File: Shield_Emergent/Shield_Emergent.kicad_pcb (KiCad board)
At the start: 2 copper layers, 33.4 x 63.5 mm, 23 parts, among them J1 Conn_01x02_Female, J2 Conn_01x04_Male, J3 Conn_01x02_Female, J4 Conn_01x04_Male, U1 Raspberri_Pi_Pico, U2 TPS2553, U3 TPS2553

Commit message: v0.9 ready to order
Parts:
- moved REF** 4.38 mm to (46.5, 82.0)
- moved REF** 3.85 mm to (28.8, 23.5)
- moved REF** 3.85 mm to (46.5, 23.5)
- moved REF** 3.76 mm to (28.8, 82.0)
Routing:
- net GND: vias 43 -> 55

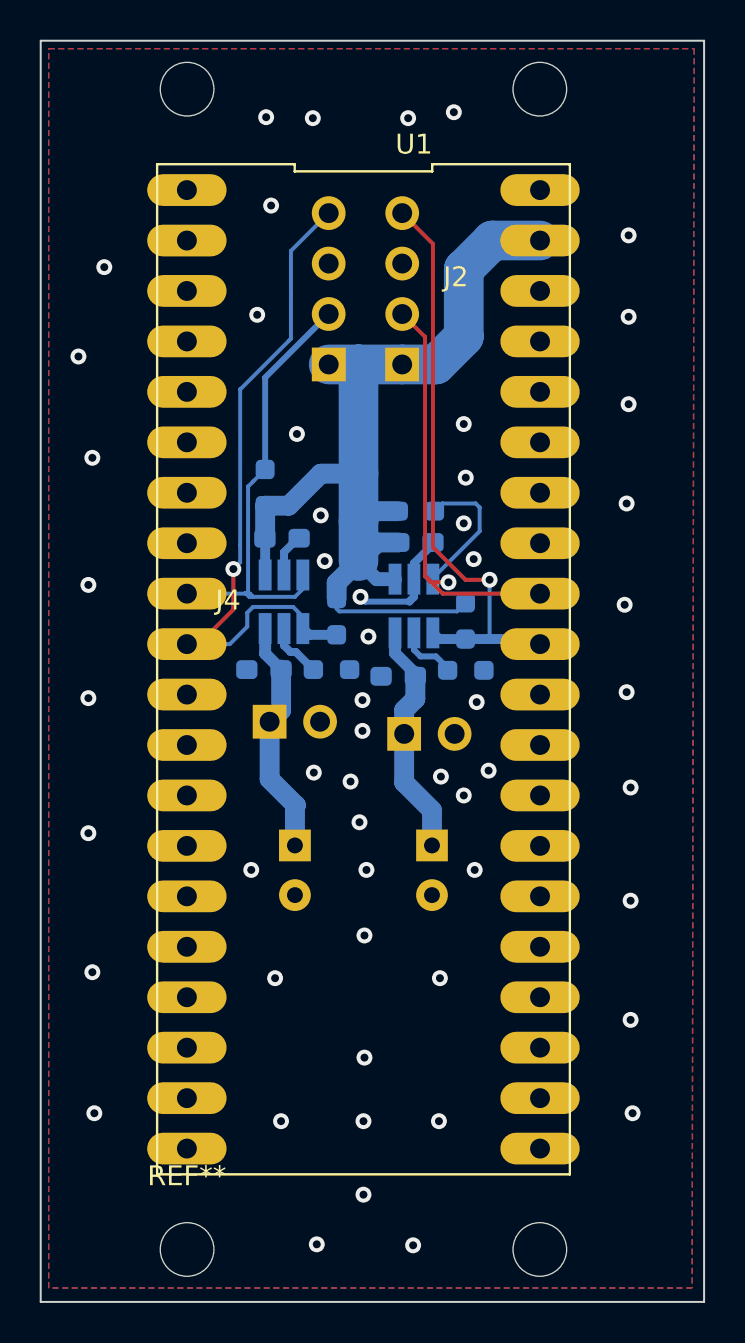
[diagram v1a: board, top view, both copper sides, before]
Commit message: v1.0 Ground was corrected
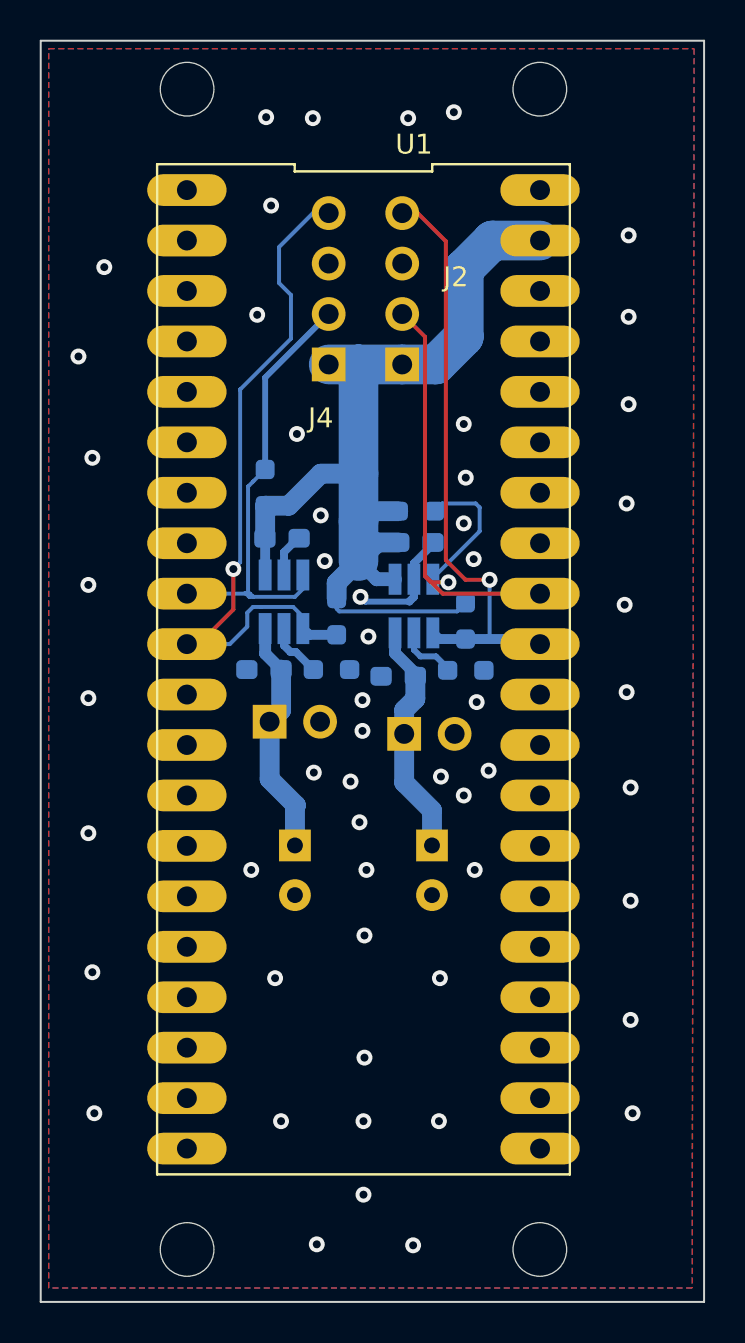
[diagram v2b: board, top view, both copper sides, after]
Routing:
- net FLT2: track 35.4 -> 36.3 mm
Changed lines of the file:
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@@
     (tags "mounting hole 2.7mm no annular m2.5")
     (attr exclude_from_pos_files exclude_from_bom)
-    (fp_text reference "REF**" (at 0 -3.7) (layer "F.SilkS")
+    (fp_text reference "REF**" (at 0 -3.7) (layer "F.SilkS") hide
       (effects (font (size 1 1) (thickness 0.15)))
     )
@@
       (effects (font (size 1 1) (thickness 0.15)))
     )
-    (fp_text user "${REFERENCE}" (at 0 -1.11) (layer "F.Fab")
+    (fp_text user "${REFERENCE}" (at 0 -1.11) (layer "F.Fab") hide
       (effects (font (size 1 1) (thickness 0.15)))
     )
@@
       (effects (font (size 1 1) (thickness 0.15)))
     )
-    (fp_text user "${REFERENCE}" (at 0 0) (layer "F.Fab")
+    (fp_text user "${REFERENCE}" (at 0 0) (layer "F.Fab") hide
       (effects (font (size 1 1) (thickness 0.15)))
     )
@@
     (property "Sheetname" "")
     (attr through_hole)
-    (fp_text reference "J4" (at -5.065 11.87) (layer "F.SilkS")
+    (fp_text reference "J4" (at -0.4 2.7) (layer "F.SilkS")
       (effects (font (size 1 1) (thickness 0.15)))
     )
@@
   (segment (start 41.6125 44.4) (end 41.225 44.7875) (width 0.2) (layer "B.Cu") (net 5))
   (segment (start 41.14 48.16) (end 43.5 45.8) (width 0.2) (layer "B.Cu") (net 5))
-  (segment (start 41.149031 46.6) (end 41.149031 31.329031) (width 0.2) (layer "F.Cu") (net 6))
-  (segment (start 41.149031 31.329031) (end 39.6 29.78) (width 0.2) (layer "F.Cu") (net 6))
-  (segment (start 42.789531 48.2405) (end 41.149031 46.6) (width 0.2) (layer "F.Cu") (net 6))
+  (segment (start 41.8 31.2) (end 40.38 29.78) (width 0.2) (layer "F.Cu") (net 6))
+  (segment (start 42.789531 48.2405) (end 41.8 47.250969) (width 0.2) (layer "F.Cu") (net 6))
+  (segment (start 41.8 47.250969) (end 41.8 31.2) (width 0.2) (layer "F.Cu") (net 6))
+  (segment (start 40.38 29.78) (end 39.6 29.78) (width 0.2) (layer "F.Cu") (net 6))
   (segment (start 44 48.2405) (end 42.789531 48.2405) (width 0.2) (layer "F.Cu") (net 6))
   (via (at 44 48.2405) (size 0.8) (drill 0.4) (layers "F.Cu" "B.Cu") (net 6))
@@
   (via (at 31.1 47.7) (size 0.8) (drill 0.4) (layers "F.Cu" "B.Cu") (net 8))
   (segment (start 31.8 50.6) (end 30.92 51.48) (width 0.2) (layer "B.Cu") (net 8))
+  (segment (start 33.4 31.49) (end 33.4 33.3) (width 0.2) (layer "B.Cu") (net 8))
   (segment (start 29.46 51.48) (end 28.76 51.48) (width 0.3) (layer "B.Cu") (net 8))
+  (segment (start 35.11 29.78) (end 33.4 31.49) (width 0.2) (layer "B.Cu") (net 8))
   (segment (start 36.3 51.0125) (end 34.9125 51.0125) (width 0.5) (layer "B.Cu") (net 8))
-  (segment (start 34 31.68) (end 34 33.9) (width 0.2) (layer "B.Cu") (net 8))
-  (segment (start 35.9 29.78) (end 34 31.68) (width 0.2) (layer "B.Cu") (net 8))
+  (segment (start 33.4 33.3) (end 34 33.9) (width 0.2) (layer "B.Cu") (net 8))
   (segment (start 34.6 50.1) (end 34.10952 49.60952) (width 0.2) (layer "B.Cu") (net 8))
   (segment (start 34.6 50.7) (end 34.6 50.1) (width 0.2) (layer "B.Cu") (net 8))
-  (segment (start 31.440481 38.659519) (end 31.44048 46.5) (width 0.2) (layer "B.Cu") (net 8))
-  (segment (start 31.44048 46.5) (end 31.44048 47.35952) (width 0.2) (layer "B.Cu") (net 8))
-  (segment (start 33.9 36.2) (end 31.440481 38.659519) (width 0.2) (layer "B.Cu") (net 8))
+  (segment (start 31.8 49.895978) (end 31.8 50.6) (width 0.2) (layer "B.Cu") (net 8))
+  (segment (start 35.9 29.78) (end 35.11 29.78) (width 0.2) (layer "B.Cu") (net 8))
   (segment (start 34 33.9) (end 34 36.1) (width 0.2) (layer "B.Cu") (net 8))
-  (segment (start 31.8 49.895978) (end 31.8 50.6) (width 0.2) (layer "B.Cu") (net 8))
-  (segment (start 34 36.1) (end 33.9 36.2) (width 0.2) (layer "B.Cu") (net 8))
+  (segment (start 34 36.1) (end 31.440481 38.659519) (width 0.2) (layer "B.Cu") (net 8))
   (segment (start 34.10952 49.60952) (end 32.49048 49.60952) (width 0.2) (layer "B.Cu") (net 8))
   (segment (start 32.49048 49.60952) (end 32.086458 49.60952) (width 0.2) (layer "B.Cu") (net 8))
   (segment (start 34.9125 51.0125) (end 34.6 50.7) (width 0.5) (layer "B.Cu") (net 8))
   (segment (start 30.92 51.48) (end 28.76 51.48) (width 0.2) (layer "B.Cu") (net 8))
+  (segment (start 31.440481 38.659519) (end 31.44048 47.35952) (width 0.2) (layer "B.Cu") (net 8))
+  (segment (start 32.086458 49.60952) (end 31.8 49.895978) (width 0.2) (layer "B.Cu") (net 8))
   (segment (start 31.44048 47.35952) (end 31.1 47.7) (width 0.2) (layer "B.Cu") (net 8))
-  (segment (start 32.086458 49.60952) (end 31.8 49.895978) (width 0.2) (layer "B.Cu") (net 8))
   (segment (start 41.3 52.1) (end 41.8875 52.6875) (width 0.3) (layer "B.Cu") (net 9))
   (segment (start 41.8875 52.6875) (end 41.8875 52.8) (width 0.3) (layer "B.Cu") (net 9))

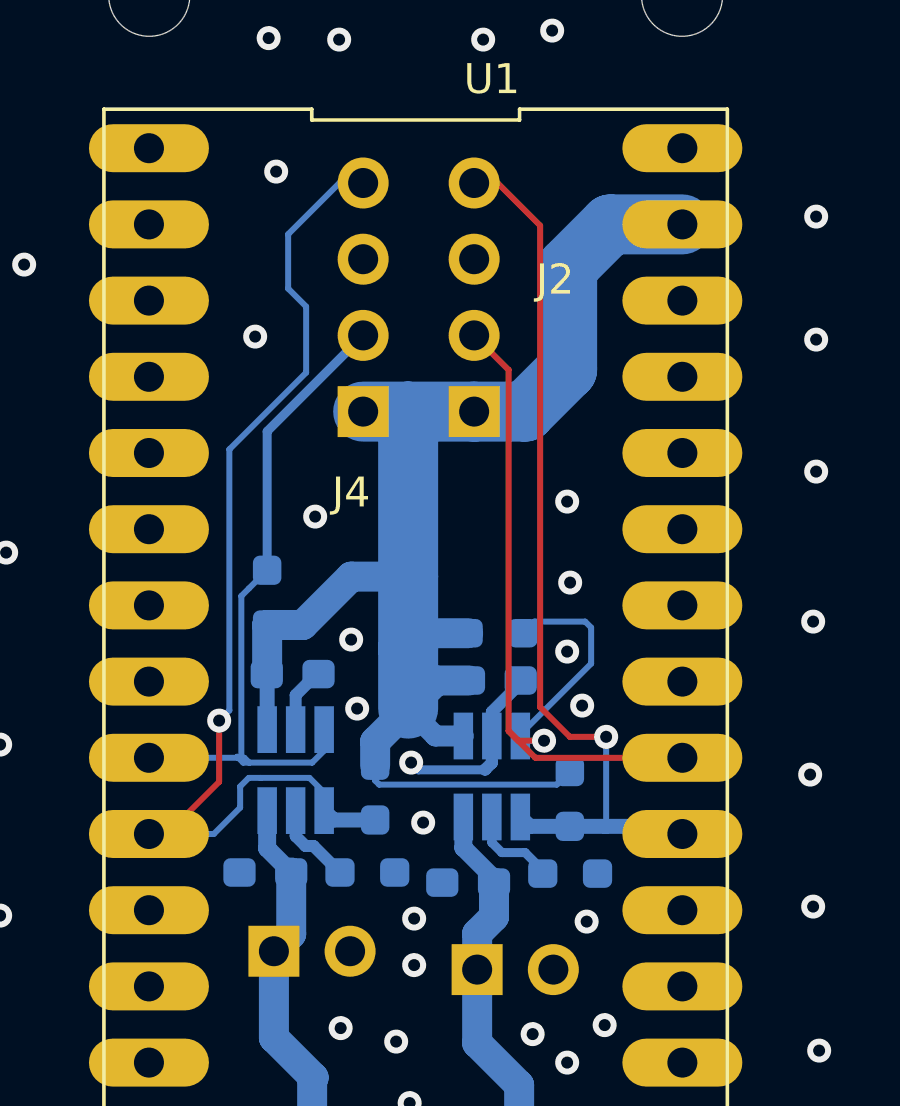
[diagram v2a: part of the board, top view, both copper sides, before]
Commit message: v1.1 Circuit was corrected, GND was enfrced
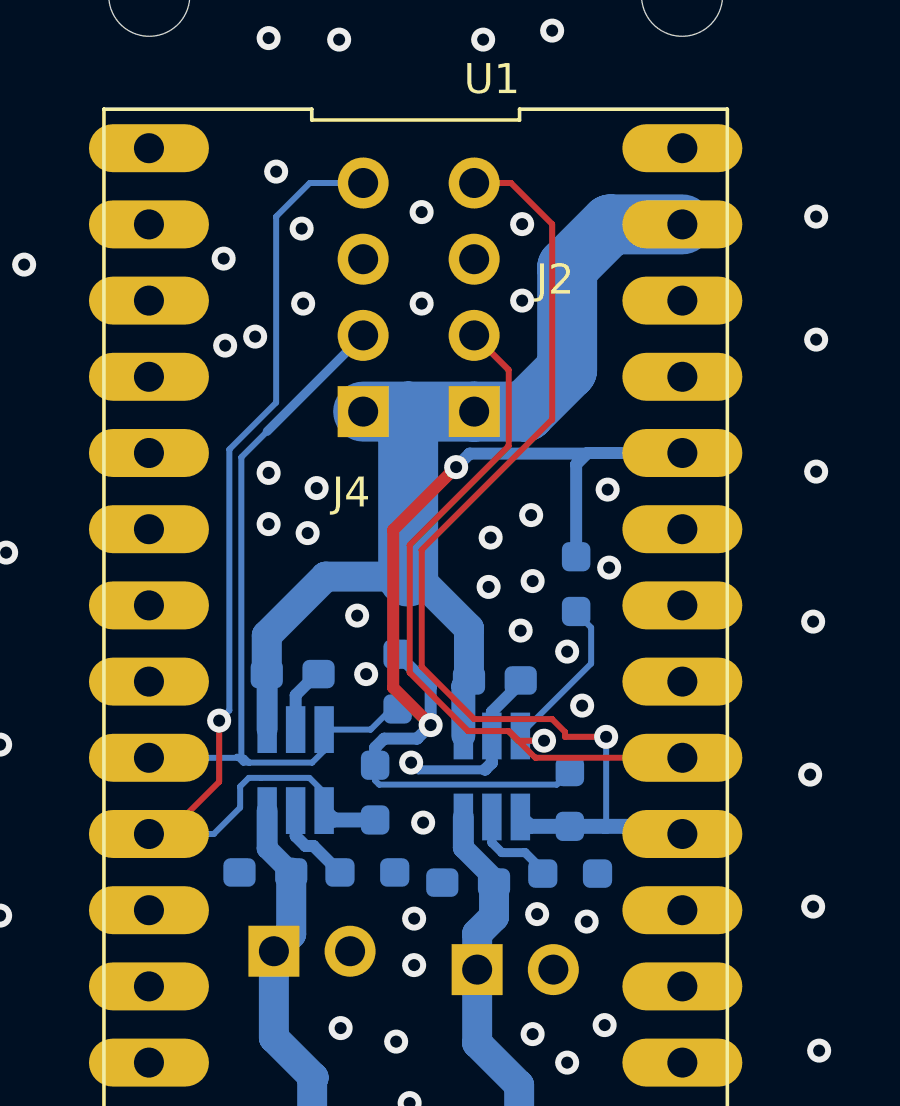
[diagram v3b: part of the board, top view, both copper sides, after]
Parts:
- moved R4 5.17 mm to (37.0, 46.4), turned to -90 degrees
- moved R1 3.15 mm to (43.0, 43.1), turned to -90 degrees
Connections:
- R1 pad 1: VBUS -> +3V3
- R3 pad 2: VBUS -> +3V3
- R4 pad 1: VBUS -> +3V3
- R6 pad 2: VBUS -> +3V3
- U1 pad 36: unconnected-(U1-Pad36) -> +3V3
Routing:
- net +3V3: track 0.00 -> 34.3 mm, vias 0 -> 2
- net VBUS: track 50.6 -> 36.0 mm
- net FLT1: track 30.1 -> 35.6 mm
- net EN2: track 23.6 -> 26.4 mm
- net EN1: track 29.1 -> 30.4 mm
- net GND: vias 55 -> 72
